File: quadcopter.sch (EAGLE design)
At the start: 62 parts, among them J1 AVR_SPI_PRG_6NS, U1 ATMEGA128RFA1

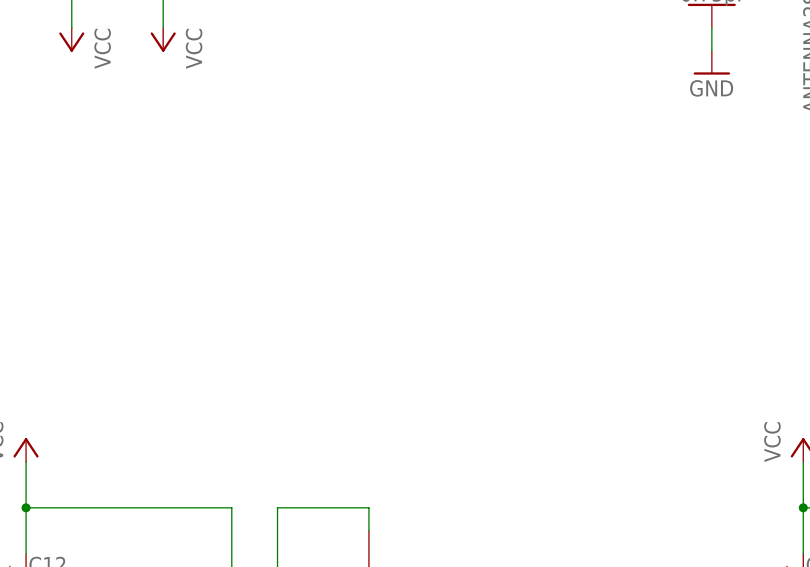
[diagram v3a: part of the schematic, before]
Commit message: Added LED to design
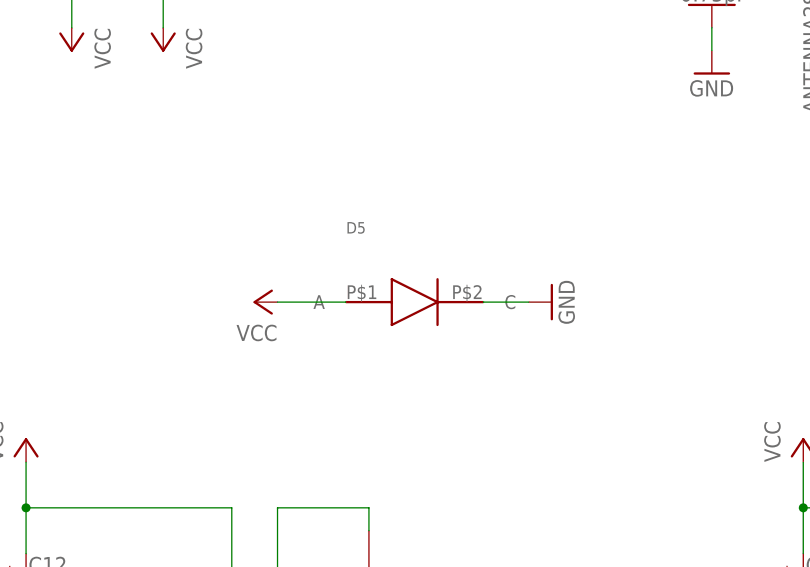
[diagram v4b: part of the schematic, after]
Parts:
- added D5: (no value), LED:BLUE_LED
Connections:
- net GND: now also D5.C
- net VCC: now also D5.A
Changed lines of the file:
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@@
 <part name="GND39" library="quadparts_prebuilt" deviceset="GND" device=""/>
 <part name="P+12" library="quadparts_prebuilt" deviceset="VCC" device=""/>
+<part name="D5" library="LED" deviceset="BLUE_LED" device=""/>
+<part name="P+13" library="quadparts_prebuilt" deviceset="VCC" device=""/>
+<part name="GND40" library="quadparts_prebuilt" deviceset="GND" device=""/>
 </parts>
 <sheets>
@@
 <instance part="GND39" gate="1" x="-45.72" y="22.86" rot="R90"/>
 <instance part="P+12" gate="VCC" x="33.02" y="53.34" rot="R270"/>
+<instance part="D5" gate="G$1" x="17.78" y="-132.08"/>
+<instance part="P+13" gate="VCC" x="-2.54" y="-132.08" rot="R90"/>
+<instance part="GND40" gate="1" x="30.48" y="-132.08" rot="R90"/>
 </instances>
 <busses>
@@
 <wire x1="-50.8" y1="22.86" x2="-48.26" y2="22.86" width="0.1524" layer="91"/>
 </segment>
+<segment>
+<pinref part="D5" gate="G$1" pin="C"/>
+<pinref part="GND40" gate="1" pin="GND"/>
+<wire x1="22.86" y1="-132.08" x2="27.94" y2="-132.08" width="0.1524" layer="91"/>
+</segment>
 </net>
 <net name="N$2" class="0">
@@
 <wire x1="12.7" y1="53.34" x2="30.48" y2="53.34" width="0.1524" layer="91"/>
 </segment>
-</net>
+<segment>
+<pinref part="P+13" gate="VCC" pin="VCC"/>
+<pinref part="D5" gate="G$1" pin="A"/>
+<wire x1="0" y1="-132.08" x2="7.62" y2="-132.08" width="0.1524" layer="91"/>
+</segment>
+</net>

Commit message: Added frame and moved all parts in schematic to fit the frame
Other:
- moved on the sheet: BATT1, C10, C12, C13, C14, C15, C16, C17, C18, C19, C20, C21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

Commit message: fixed gnd->bat_gnd for all motor parts. also flipped source and drain
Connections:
- net BAT_GND: now also C12.-, C14.-, C17.-, C8.-, Q1.S, Q2.S, Q3.S, Q4.S; no longer Q1.D, Q2.D, Q3.D, Q4.D
- net FLYBACK: now also Q1.D, Q2.D, Q3.D, Q4.D; no longer Q1.S, Q2.S, Q3.S, Q4.S
- net GND: no longer C12.-, C14.-, C17.-, C8.-
- net VBAT: now also D5.A
- net VCC: no longer D5.A
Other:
- moved on the sheet: D5

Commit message: Made all the review changes
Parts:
- removed D2, D3, D4: RED, quadparts-nick:RED_LED
- added D6, D7, D8: 360mV, quadparts_prebuilt:DIODE-SCHOTTKY_SMD-SOD123-360MV
- added R12, R13: 10K, quadparts_prebuilt:RESISTOR_SMD-2012-0805-10K
- D1: value RED -> 360mV; device quadparts-nick:RED_LED -> quadparts_prebuilt:DIODE-SCHOTTKY_SMD-SOD123-360MV
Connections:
- new net N$16: IMU.SDA/I/O, R13.2
- new net N$19: IMU.SCL/SPC, R12.2
- net FLYBACK: now also D6.A, D7.A, D8.A; no longer D2.A, D3.A, D4.A
- net GND: now also IMU.SDO_M
- net SCL: now also R12.1; no longer IMU.SCL/SPC
- net SDA: now also R13.1; no longer IMU.SDA/I/O
- net VBAT: now also C12.+, C14.+, C17.+, C8.+, D1.C, D6.C, D7.C, D8.C, U$1.V+, U$2.V+, U$3.V+, U$4.V+
- net VCC: now also IMU.DEN_A/G, IMU.SDO_A/G; no longer C12.+, C14.+, C17.+, C8.+, D1.C, D2.C, D3.C, D4.C, U$1.V+, U$2.V+, U$3.V+, U$4.V+

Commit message: Made changes according to Profs feedback
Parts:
- C10, C13, C16, C7: value 1uF -> 0.1uF; device quadparts_prebuilt:CAPACITOR-NP_SMD-2012-0805_CERAMIC-1UF -> quadparts_prebuilt:CAPACITOR-NP_SMD-2012-0805_CERAMIC-0.1UF
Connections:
- removed net N$16: IMU.SDA/I/O, R13.2
- removed net N$19: IMU.SCL/SPC, R12.2
- net SCL: now also IMU.SCL/SPC, R12.2; no longer R12.1
- net SDA: now also IMU.SDA/I/O, R13.2; no longer R13.1
- net VCC: now also R12.1, R13.1
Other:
- moved on the sheet: R12, R13
